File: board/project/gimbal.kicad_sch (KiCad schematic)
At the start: 7 parts, among them M1 Motor_Servo, M2 Motor_Servo, U1 LM7805_TO220, U2 GY-521, U3 Joystick

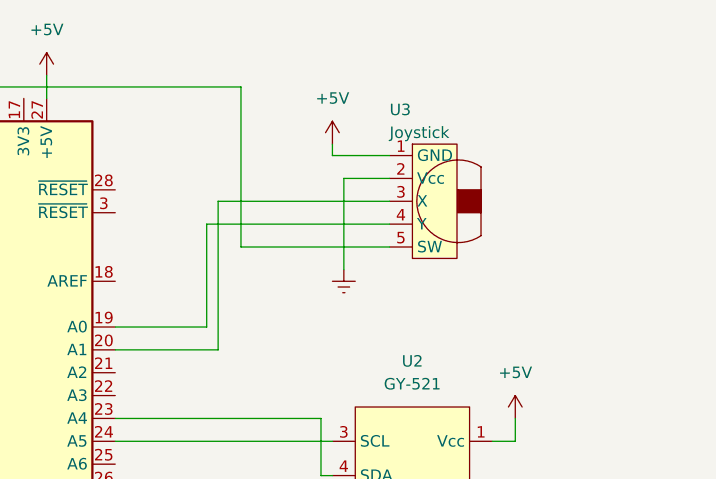
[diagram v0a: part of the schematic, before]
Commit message: fix joystick power input
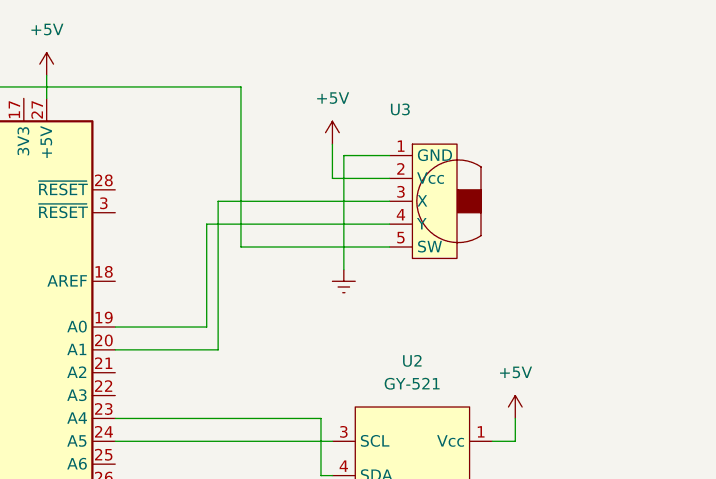
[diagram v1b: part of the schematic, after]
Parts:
- U3: value Joystick -> (none); footprint Connector_PinHeader_2.54mm:PinHeader_1x05_P2.54mm_Vertical -> (none)
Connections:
- net +5V: now also U3.2 (Vcc); no longer U3.1 (GND)
- net Earth: now also U3.1 (GND); no longer U3.2 (Vcc)
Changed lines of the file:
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@@
+    (stroke (width 0) (type default) (color 0 0 0 0))
+  )
+  (wire (pts (xy 204.47 76.2) (xy 198.12 76.2))
     (stroke (width 0) (type default) (color 0 0 0 0))
   )
@@
     (stroke (width 0) (type default) (color 0 0 0 0))
   )
+  (wire (pts (xy 199.39 73.66) (xy 204.47 73.66))
+    (stroke (width 0) (type default) (color 0 0 0 0))
+  )
   (wire (pts (xy 107.95 91.44) (xy 115.57 91.44))
     (stroke (width 0) (type default) (color 0 0 0 0))
@@
     (stroke (width 0) (type default) (color 0 0 0 0))
   )
-  (wire (pts (xy 199.39 76.2) (xy 199.39 86.36))
+  (wire (pts (xy 199.39 73.66) (xy 199.39 86.36))
     (stroke (width 0) (type default) (color 0 0 0 0))
   )
@@
     (stroke (width 0) (type default) (color 0 0 0 0))
   )
-  (wire (pts (xy 198.12 72.39) (xy 198.12 73.66))
+  (wire (pts (xy 198.12 72.39) (xy 198.12 76.2))
     (stroke (width 0) (type default) (color 0 0 0 0))
   )
@@
   )
   (wire (pts (xy 114.3 88.9) (xy 115.57 88.9))
-    (stroke (width 0) (type default) (color 0 0 0 0))
-  )
-  (wire (pts (xy 204.47 76.2) (xy 199.39 76.2))
     (stroke (width 0) (type default) (color 0 0 0 0))
   )
@@
     (stroke (width 0) (type default) (color 0 0 0 0))
   )
-  (wire (pts (xy 198.12 73.66) (xy 204.47 73.66))
-    (stroke (width 0) (type default) (color 0 0 0 0))
-  )
   (wire (pts (xy 198.12 109.22) (xy 196.85 109.22))
     (stroke (width 0) (type default) (color 0 0 0 0))
@@
       (effects (font (size 1.27 1.27)) (justify left))
     )
-    (property "Value" "Joystick" (id 1) (at 204.47 71.12 0)
+    (property "Value" "" (id 1) (at 204.47 71.12 0)
       (effects (font (size 1.27 1.27)) (justify left))
     )
-    (property "Footprint" "Connector_PinHeader_2.54mm:PinHeader_1x05_P2.54mm_Vertical" (id 2) (at 203.962 62.992 0)
+    (property "Footprint" "" (id 2) (at 203.962 62.992 0)
       (effects (font (size 1.27 1.27)) hide)
     )
